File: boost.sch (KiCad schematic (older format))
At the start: 12 parts, among them SW1 SW_SPST, U2 TPS61022

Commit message: Rename to Sailor Hat
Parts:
- U2: symbol pi-supercap-ups:TPS61022 -> sailor-hat-rescue:TPS61022-sailor-hat
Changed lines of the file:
@@
-EESchema Schematic File Version 5
-LIBS:pi-supercap-ups-cache
+EESchema Schematic File Version 4
 EELAYER 30 0
 EELAYER END
@@
 Comment3 ""
 Comment4 ""
-Comment5 ""
-Comment6 ""
-Comment7 ""
-Comment8 ""
-Comment9 ""
 $EndDescr
 $Comp
@@
 $EndComp
 $Comp
-L pi-supercap-ups:TPS61022 U2
+L sailor-hat-rescue:TPS61022-sailor-hat U2
 U 1 1 5D5AC086
 P 3400 2400

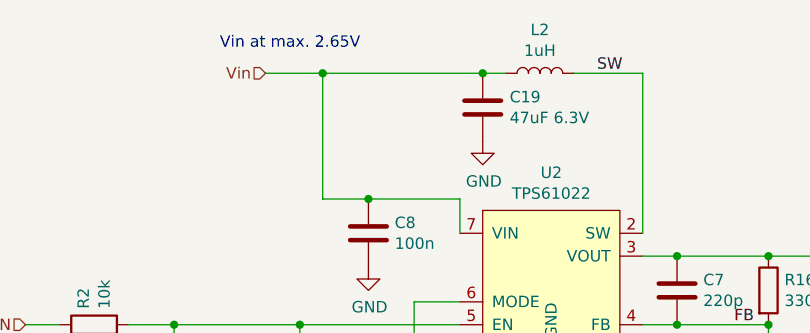
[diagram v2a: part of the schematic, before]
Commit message: Annotate and tweak power flags
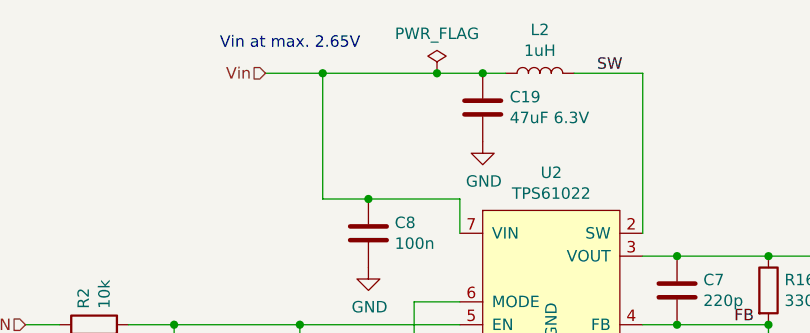
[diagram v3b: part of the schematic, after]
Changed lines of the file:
@@
 	3000 2050 2600 2050
 Wire Wire Line
-	2400 1500 3100 1500
+	2400 1500 2900 1500
 Wire Wire Line
 	3800 1500 3500 1500
@@
 	1    0    0    -1
 $EndComp
+$Comp
+L power:PWR_FLAG #FLG0101
+U 1 1 5E2AF28D
+P 2900 1500
+F 0 "#FLG0101" H 2900 1575 50  0001 C CNN
+F 1 "PWR_FLAG" H 2900 1673 50  0000 C CNN
+F 2 "" H 2900 1500 50  0001 C CNN
+F 3 "~" H 2900 1500 50  0001 C CNN
+	1    2900 1500
+	1    0    0    -1
+$EndComp
+Connection ~ 2900 1500
+Wire Wire Line
+	2900 1500 3100 1500
 $EndSCHEMATC

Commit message: Update licence, tweaks to footprints and ERC
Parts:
- C17, C19, C6: footprint Capacitor_SMD:C_0805_2012Metric_Pad1.15x1.40mm_HandSolder -> Capacitor_SMD:C_1210_3225Metric
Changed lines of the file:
@@
 $Descr A4 11693 8268
 encoding utf-8
-Sheet 3 6
+Sheet 3 7
 Title ""
 Date ""
@@
 F 0 "C17" H 4968 2496 50  0000 L CNN
 F 1 "47uF 10V" H 4968 2405 50  0000 L CNN
-F 2 "Capacitor_SMD:C_0805_2012Metric_Pad1.15x1.40mm_HandSolder" H 4888 2300 50  0001 C CNN
+F 2 "Capacitor_SMD:C_1210_3225Metric" H 4888 2300 50  0001 C CNN
 F 3 "~" H 4850 2450 50  0001 C CNN
 	1    4850 2450
@@
 F 0 "C19" H 3218 1696 50  0000 L CNN
 F 1 "47uF 6.3V" H 3218 1605 50  0000 L CNN
-F 2 "Capacitor_SMD:C_0805_2012Metric_Pad1.15x1.40mm_HandSolder" H 3138 1500 50  0001 C CNN
+F 2 "Capacitor_SMD:C_1210_3225Metric" H 3138 1500 50  0001 C CNN
 F 3 "~" H 3100 1650 50  0001 C CNN
 	1    3100 1650
@@
 F 0 "C6" H 5568 2496 50  0000 L CNN
 F 1 "47uF 10V" H 5568 2405 50  0000 L CNN
-F 2 "Capacitor_SMD:C_0805_2012Metric_Pad1.15x1.40mm_HandSolder" H 5488 2300 50  0001 C CNN
+F 2 "Capacitor_SMD:C_1210_3225Metric" H 5488 2300 50  0001 C CNN
 F 3 "~" H 5450 2450 50  0001 C CNN
 	1    5450 2450

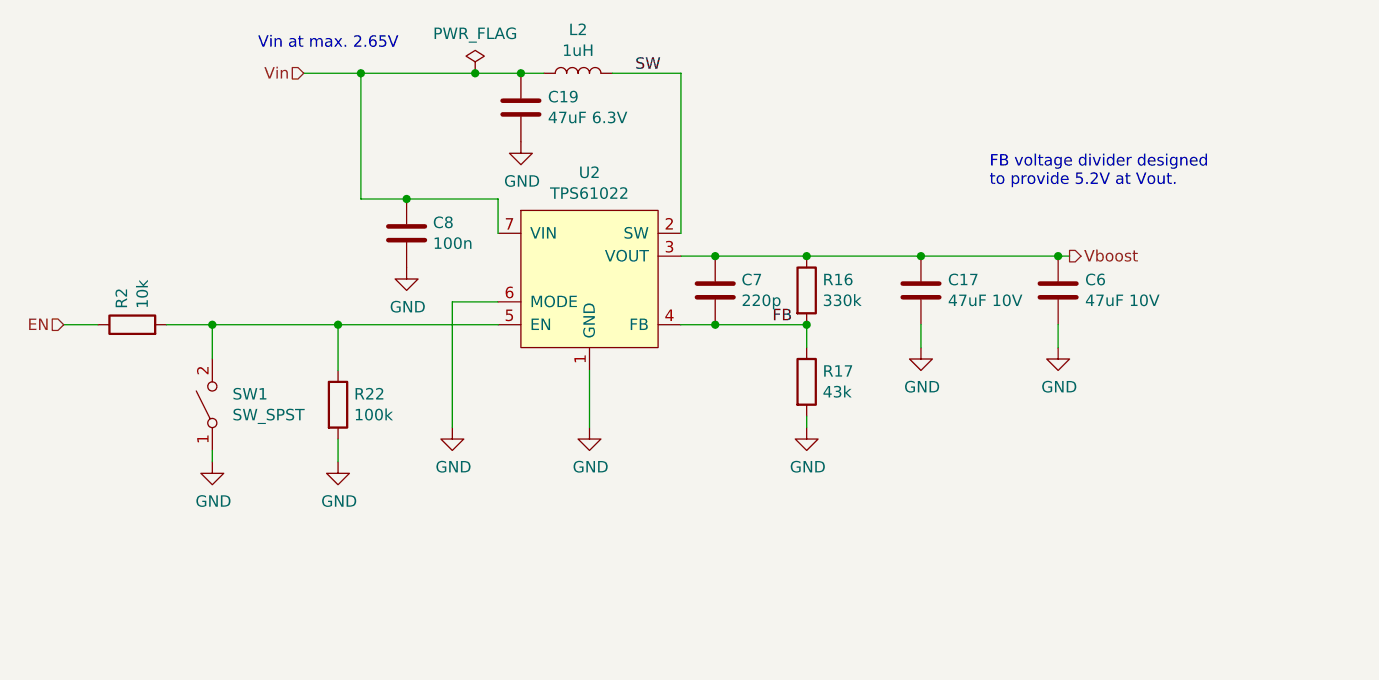
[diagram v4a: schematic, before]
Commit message: Add LCSC part numbers to components
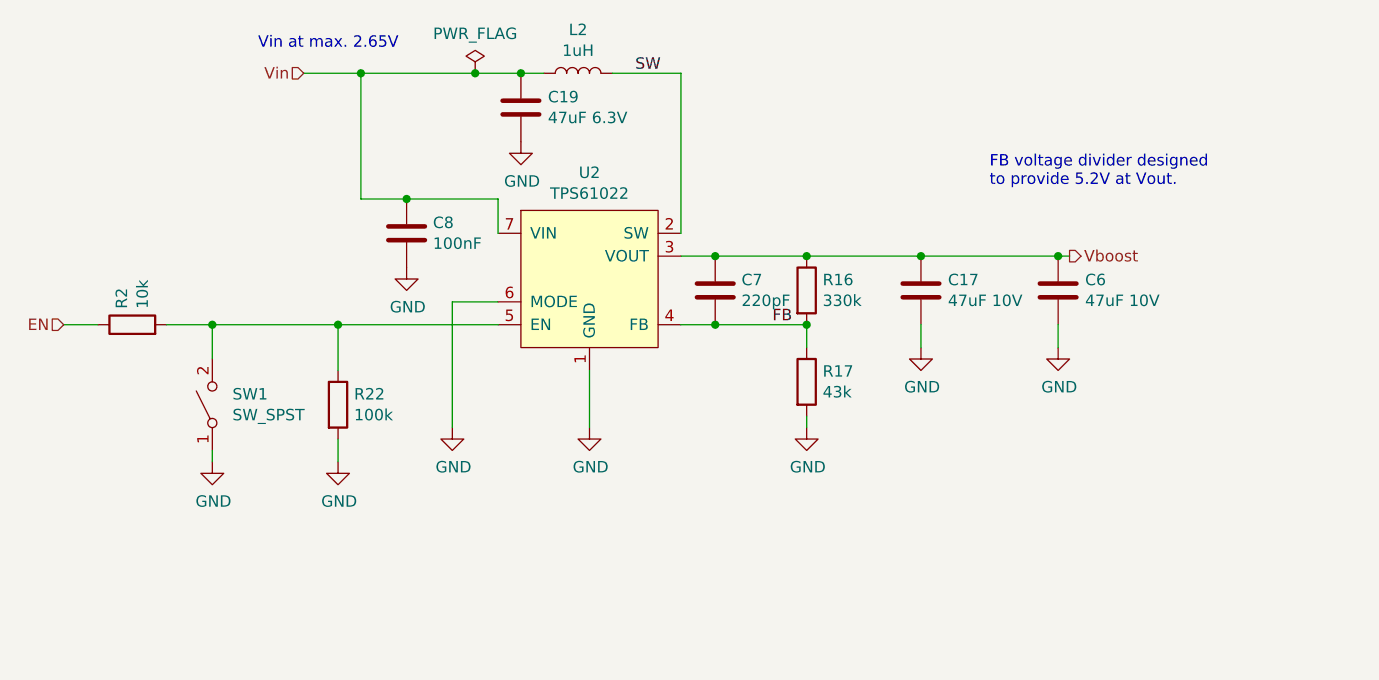
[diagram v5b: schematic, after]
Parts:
- C17, C19, C6: LCSC (none) -> C77101
- C7: value 220p -> 220pF; LCSC (none) -> C1603
- C8: value 100n -> 100nF; LCSC (none) -> C14663
- L2: LCSC (none) -> C112125
- R16: LCSC (none) -> C23137
- R17: LCSC (none) -> C23172
- R2: LCSC (none) -> C25804
- R22: LCSC (none) -> C25803
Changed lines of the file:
@@
 F 2 "Capacitor_SMD:C_1210_3225Metric" H 4888 2300 50  0001 C CNN
 F 3 "~" H 4850 2450 50  0001 C CNN
+F 4 "C77101" H 4850 2450 50  0001 C CNN "LCSC"
 	1    4850 2450
 	1    0    0    -1
@@
 F 3 "" H 3350 1500 50  0001 C CNN
 F 4 "Shun Xiang Nuo Elec SMMS0630-1R0M" V 3350 1500 50  0001 C CNN "Notes"
+F 5 "C112125" H 3350 1500 50  0001 C CNN "LCSC"
 	1    3350 1500
 	0    -1   -1   0
@@
 F 2 "Resistor_SMD:R_0603_1608Metric_Pad1.05x0.95mm_HandSolder" V 4280 2450 50  0001 C CNN
 F 3 "~" H 4350 2450 50  0001 C CNN
+F 4 "C23137" H 4350 2450 50  0001 C CNN "LCSC"
 	1    4350 2450
 	1    0    0    -1
@@
 F 2 "Resistor_SMD:R_0603_1608Metric_Pad1.05x0.95mm_HandSolder" V 4280 2850 50  0001 C CNN
 F 3 "~" H 4350 2850 50  0001 C CNN
+F 4 "C23172" H 4350 2850 50  0001 C CNN "LCSC"
 	1    4350 2850
 	1    0    0    -1
@@
 F 2 "Capacitor_SMD:C_1210_3225Metric" H 3138 1500 50  0001 C CNN
 F 3 "~" H 3100 1650 50  0001 C CNN
+F 4 "C77101" H 3100 1650 50  0001 C CNN "LCSC"
 	1    3100 1650
 	1    0    0    -1
@@
 F 2 "Resistor_SMD:R_0603_1608Metric_Pad1.05x0.95mm_HandSolder" V 1330 2600 50  0001 C CNN
 F 3 "~" H 1400 2600 50  0001 C CNN
+F 4 "C25804" H 1400 2600 50  0001 C CNN "LCSC"
 	1    1400 2600
 	0    -1   -1   0
@@
 F 2 "Capacitor_SMD:C_1210_3225Metric" H 5488 2300 50  0001 C CNN
 F 3 "~" H 5450 2450 50  0001 C CNN
+F 4 "C77101" H 5450 2450 50  0001 C CNN "LCSC"
 	1    5450 2450
 	1    0    0    -1
@@
 P 3950 2450
 F 0 "C7" H 4065 2496 50  0000 L CNN
-F 1 "220p" H 4065 2405 50  0000 L CNN
+F 1 "220pF" H 4065 2405 50  0000 L CNN
 F 2 "Capacitor_SMD:C_0603_1608Metric_Pad1.05x0.95mm_HandSolder" H 3988 2300 50  0001 C CNN
 F 3 "~" H 3950 2450 50  0001 C CNN
+F 4 "C1603" H 3950 2450 50  0001 C CNN "LCSC"
 	1    3950 2450
 	1    0    0    -1
@@
 F 2 "Resistor_SMD:R_0603_1608Metric_Pad1.05x0.95mm_HandSolder" V 2230 2950 50  0001 C CNN
 F 3 "~" H 2300 2950 50  0001 C CNN
+F 4 "C25803" H 2300 2950 50  0001 C CNN "LCSC"
 	1    2300 2950
 	1    0    0    -1
@@
 P 2600 2200
 F 0 "C8" H 2715 2246 50  0000 L CNN
-F 1 "100n" H 2715 2155 50  0000 L CNN
+F 1 "100nF" H 2715 2155 50  0000 L CNN
 F 2 "Capacitor_SMD:C_0603_1608Metric_Pad1.05x0.95mm_HandSolder" H 2638 2050 50  0001 C CNN
 F 3 "~" H 2600 2200 50  0001 C CNN
+F 4 "C14663" H 2600 2200 50  0001 C CNN "LCSC"
 	1    2600 2200
 	1    0    0    -1

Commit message: Update parts according to JLCPCB availability
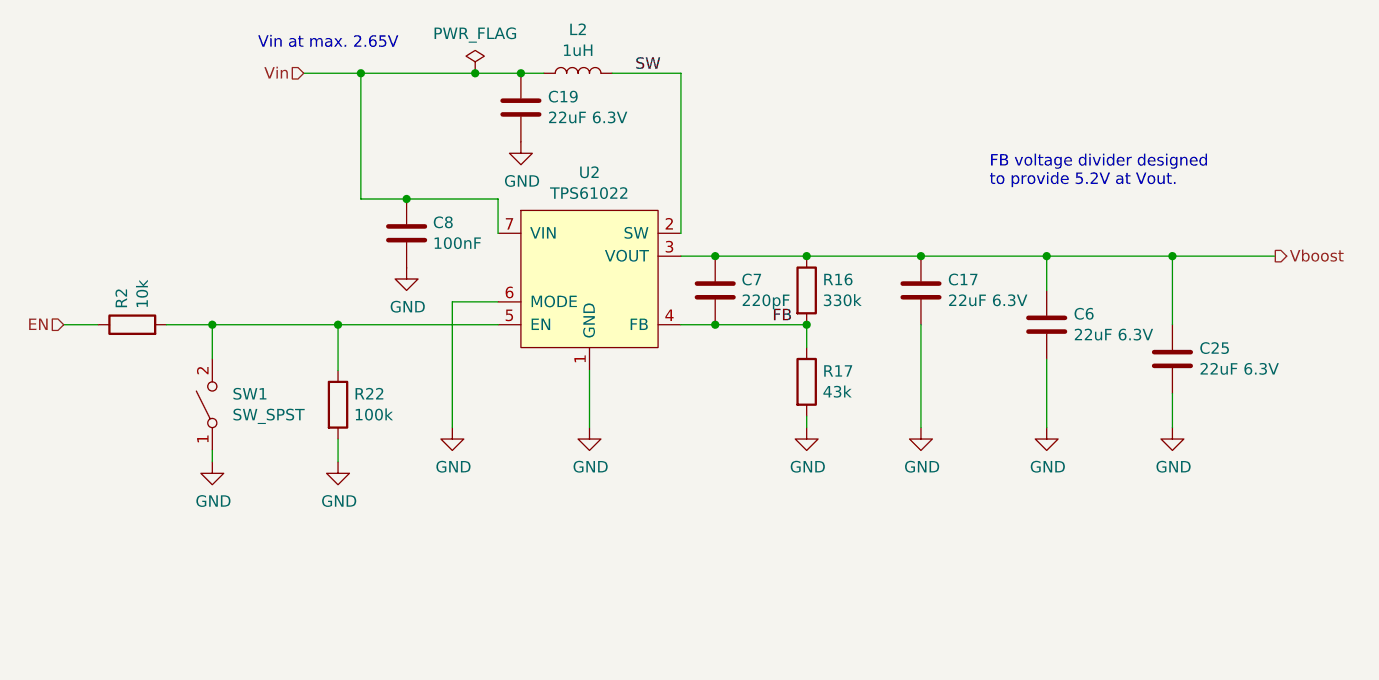
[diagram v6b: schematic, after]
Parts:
- added C25: 22uF 6.3V, Capacitor_SMD:C_0805_2012Metric_Pad1.15x1.40mm_HandSolder, symbol Device:C
- C17, C6: value 47uF 10V -> 22uF 6.3V; footprint Capacitor_SMD:C_1210_3225Metric -> Capacitor_SMD:C_0805_2012Metric_Pad1.15x1.40mm_HandSolder; LCSC C77101 -> C45783
- C19: value 47uF 6.3V -> 22uF 6.3V; footprint Capacitor_SMD:C_1210_3225Metric -> Capacitor_SMD:C_0805_2012Metric_Pad1.15x1.40mm_HandSolder; LCSC C77101 -> C45783
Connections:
- net GND: now also C25.2
- net Vboost: now also C25.1
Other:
- moved on the sheet: C6
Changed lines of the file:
@@
 AR Path="/5CA73F16/5CA6B4E8" Ref="C17"  Part="1"
 F 0 "C17" H 4968 2496 50  0000 L CNN
-F 1 "47uF 10V" H 4968 2405 50  0000 L CNN
-F 2 "Capacitor_SMD:C_1210_3225Metric" H 4888 2300 50  0001 C CNN
+F 1 "22uF 6.3V" H 4968 2405 50  0000 L CNN
+F 2 "Capacitor_SMD:C_0805_2012Metric_Pad1.15x1.40mm_HandSolder" H 4888 2300 50  0001 C CNN
 F 3 "~" H 4850 2450 50  0001 C CNN
-F 4 "C77101" H 4850 2450 50  0001 C CNN "LCSC"
+F 4 "C45783" H 4850 2450 50  0001 C CNN "LCSC"
 	1    4850 2450
-	1    0    0    -1
-$EndComp
-$Comp
-L power:GND #PWR?
-U 1 1 5CA6B4EF
-P 4850 2700
-AR Path="/5CA6B4EF" Ref="#PWR?"  Part="1"
-AR Path="/5C3480BB/5CA6B4EF" Ref="#PWR?"  Part="1"
-AR Path="/5CA73F16/5CA6B4EF" Ref="#PWR046"  Part="1"
-F 0 "#PWR046" H 4850 2450 50  0001 C CNN
-F 1 "GND" H 4855 2527 50  0000 C CNN
-F 2 "" H 4850 2700 50  0001 C CNN
-F 3 "" H 4850 2700 50  0001 C CNN
-	1    4850 2700
 	1    0    0    -1
 $EndComp
@@
 	4350 3050 4350 3000
 Wire Wire Line
-	4850 2700 4850 2600
-Wire Wire Line
 	2150 1500 2400 1500
 Text Label 3600 1500 0    50   ~ 0
@@
 Text Notes 5150 2000 0    50   ~ 0
 FB voltage divider designed\nto provide 5.2V at Vout.
-Text HLabel 5500 2300 2    50   Output ~ 0
+Text HLabel 6400 2300 2    50   Output ~ 0
 Vboost
 $Comp
@@
 AR Path="/5CA73F16/5CF608F8" Ref="C19"  Part="1"
 F 0 "C19" H 3218 1696 50  0000 L CNN
-F 1 "47uF 6.3V" H 3218 1605 50  0000 L CNN
-F 2 "Capacitor_SMD:C_1210_3225Metric" H 3138 1500 50  0001 C CNN
+F 1 "22uF 6.3V" H 3218 1605 50  0000 L CNN
+F 2 "Capacitor_SMD:C_0805_2012Metric_Pad1.15x1.40mm_HandSolder" H 3138 1500 50  0001 C CNN
 F 3 "~" H 3100 1650 50  0001 C CNN
-F 4 "C77101" H 3100 1650 50  0001 C CNN "LCSC"
+F 4 "C45783" H 3100 1650 50  0001 C CNN "LCSC"
 	1    3100 1650
 	1    0    0    -1
@@
 Wire Wire Line
 	3800 2300 3950 2300
-Wire Wire Line
-	5500 2300 5450 2300
 Connection ~ 4350 2300
 Connection ~ 4850 2300
@@
 L Device:C C?
 U 1 1 5D8155D9
-P 5450 2450
+P 5400 2600
 AR Path="/5D8155D9" Ref="C?"  Part="1"
 AR Path="/5C3480BB/5D8155D9" Ref="C?"  Part="1"
 AR Path="/5CA73F16/5D8155D9" Ref="C6"  Part="1"
-F 0 "C6" H 5568 2496 50  0000 L CNN
-F 1 "47uF 10V" H 5568 2405 50  0000 L CNN
-F 2 "Capacitor_SMD:C_1210_3225Metric" H 5488 2300 50  0001 C CNN
-F 3 "~" H 5450 2450 50  0001 C CNN
-F 4 "C77101" H 5450 2450 50  0001 C CNN "LCSC"
-	1    5450 2450
-	1    0    0    -1
-$EndComp
-Connection ~ 5450 2300
-Wire Wire Line
-	5450 2300 4850 2300
-$Comp
-L power:GND #PWR?
-U 1 1 5D815A89
-P 5450 2700
-AR Path="/5D815A89" Ref="#PWR?"  Part="1"
-AR Path="/5C3480BB/5D815A89" Ref="#PWR?"  Part="1"
-AR Path="/5CA73F16/5D815A89" Ref="#PWR024"  Part="1"
-F 0 "#PWR024" H 5450 2450 50  0001 C CNN
-F 1 "GND" H 5455 2527 50  0000 C CNN
-F 2 "" H 5450 2700 50  0001 C CNN
-F 3 "" H 5450 2700 50  0001 C CNN
-	1    5450 2700
-	1    0    0    -1
-$EndComp
-Wire Wire Line
-	5450 2600 5450 2700
+F 0 "C6" H 5518 2646 50  0000 L CNN
+F 1 "22uF 6.3V" H 5518 2555 50  0000 L CNN
+F 2 "Capacitor_SMD:C_0805_2012Metric_Pad1.15x1.40mm_HandSolder" H 5438 2450 50  0001 C CNN
+F 3 "~" H 5400 2600 50  0001 C CNN
+F 4 "C45783" H 5400 2600 50  0001 C CNN "LCSC"
+	1    5400 2600
+	1    0    0    -1
+$EndComp
 Wire Wire Line
 	2800 3050 2800 2500
@@
 Wire Wire Line
 	2900 1500 3100 1500
+Wire Wire Line
+	5400 2450 5400 2300
+Connection ~ 5400 2300
+Wire Wire Line
+	5400 2300 4850 2300
+Wire Wire Line
+	5400 2300 5950 2300
+$Comp
+L Device:C C?
+U 1 1 5E6767E0
+P 5950 2750
+AR Path="/5E6767E0" Ref="C?"  Part="1"
+AR Path="/5C3480BB/5E6767E0" Ref="C?"  Part="1"
+AR Path="/5CA73F16/5E6767E0" Ref="C25"  Part="1"
+F 0 "C25" H 6068 2796 50  0000 L CNN
+F 1 "22uF 6.3V" H 6068 2705 50  0000 L CNN
+F 2 "Capacitor_SMD:C_0805_2012Metric_Pad1.15x1.40mm_HandSolder" H 5988 2600 50  0001 C CNN
+F 3 "~" H 5950 2750 50  0001 C CNN
+F 4 "C45783" H 5950 2750 50  0001 C CNN "LCSC"
+	1    5950 2750
+	1    0    0    -1
+$EndComp
+Wire Wire Line
+	5950 2600 5950 2300
+Connection ~ 5950 2300
+Wire Wire Line
+	5950 2300 6400 2300
+Wire Wire Line
+	5950 2900 5950 3050
+$Comp
+L power:GND #PWR?
+U 1 1 5E6767E6
+P 5950 3050
+AR Path="/5E6767E6" Ref="#PWR?"  Part="1"
+AR Path="/5C3480BB/5E6767E6" Ref="#PWR?"  Part="1"
+AR Path="/5CA73F16/5E6767E6" Ref="#PWR058"  Part="1"
+F 0 "#PWR058" H 5950 2800 50  0001 C CNN
+F 1 "GND" H 5955 2877 50  0000 C CNN
+F 2 "" H 5950 3050 50  0001 C CNN
+F 3 "" H 5950 3050 50  0001 C CNN
+	1    5950 3050
+	1    0    0    -1
+$EndComp
+Wire Wire Line
+	5400 2750 5400 3050
+$Comp
+L power:GND #PWR?
+U 1 1 5D815A89
+P 5400 3050
+AR Path="/5D815A89" Ref="#PWR?"  Part="1"
+AR Path="/5C3480BB/5D815A89" Ref="#PWR?"  Part="1"
+AR Path="/5CA73F16/5D815A89" Ref="#PWR024"  Part="1"
+F 0 "#PWR024" H 5400 2800 50  0001 C CNN
+F 1 "GND" H 5405 2877 50  0000 C CNN
+F 2 "" H 5400 3050 50  0001 C CNN
+F 3 "" H 5400 3050 50  0001 C CNN
+	1    5400 3050
+	1    0    0    -1
+$EndComp
+$Comp
+L power:GND #PWR?
+U 1 1 5CA6B4EF
+P 4850 3050
+AR Path="/5CA6B4EF" Ref="#PWR?"  Part="1"
+AR Path="/5C3480BB/5CA6B4EF" Ref="#PWR?"  Part="1"
+AR Path="/5CA73F16/5CA6B4EF" Ref="#PWR046"  Part="1"
+F 0 "#PWR046" H 4850 2800 50  0001 C CNN
+F 1 "GND" H 4855 2877 50  0000 C CNN
+F 2 "" H 4850 3050 50  0001 C CNN
+F 3 "" H 4850 3050 50  0001 C CNN
+	1    4850 3050
+	1    0    0    -1
+$EndComp
+Wire Wire Line
+	4850 3050 4850 2600
 $EndSCHEMATC
